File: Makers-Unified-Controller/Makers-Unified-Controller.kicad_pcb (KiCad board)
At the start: 2 copper layers, 160 x 83.8 mm, 62 parts, among them J1 USB_B_Micro, J2 backup_PROG, Q1 SI2305B-TP, Q2 MMBT3904, Q3 MMBT3904, SW1 SW_DPDT_x2, SW10 SW_Push, SW11 SW_Push, SW12 SW_Push, SW13 SW_Push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

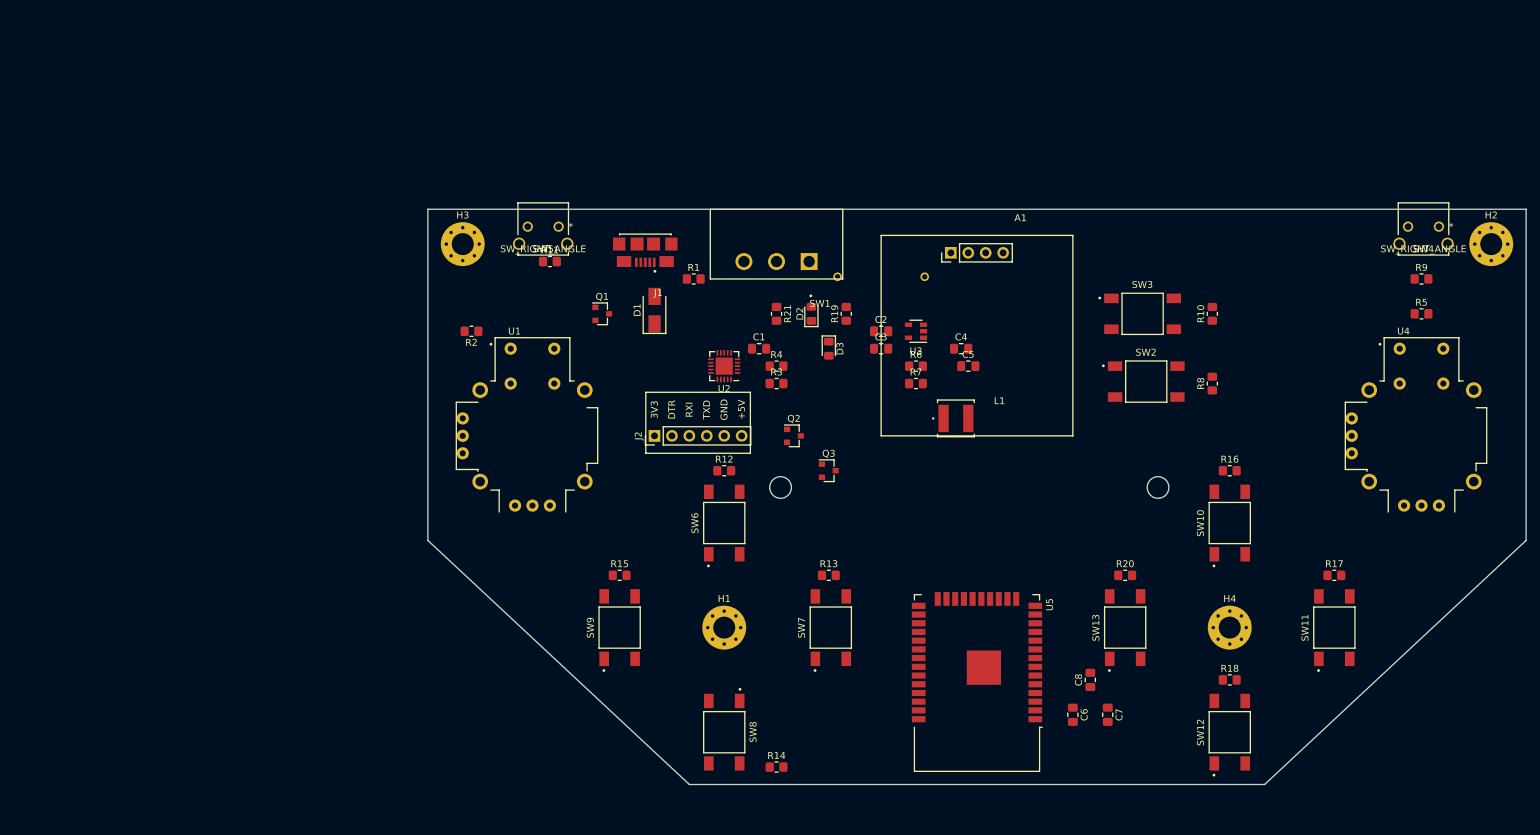
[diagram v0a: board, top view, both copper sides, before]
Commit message: Compacted layout
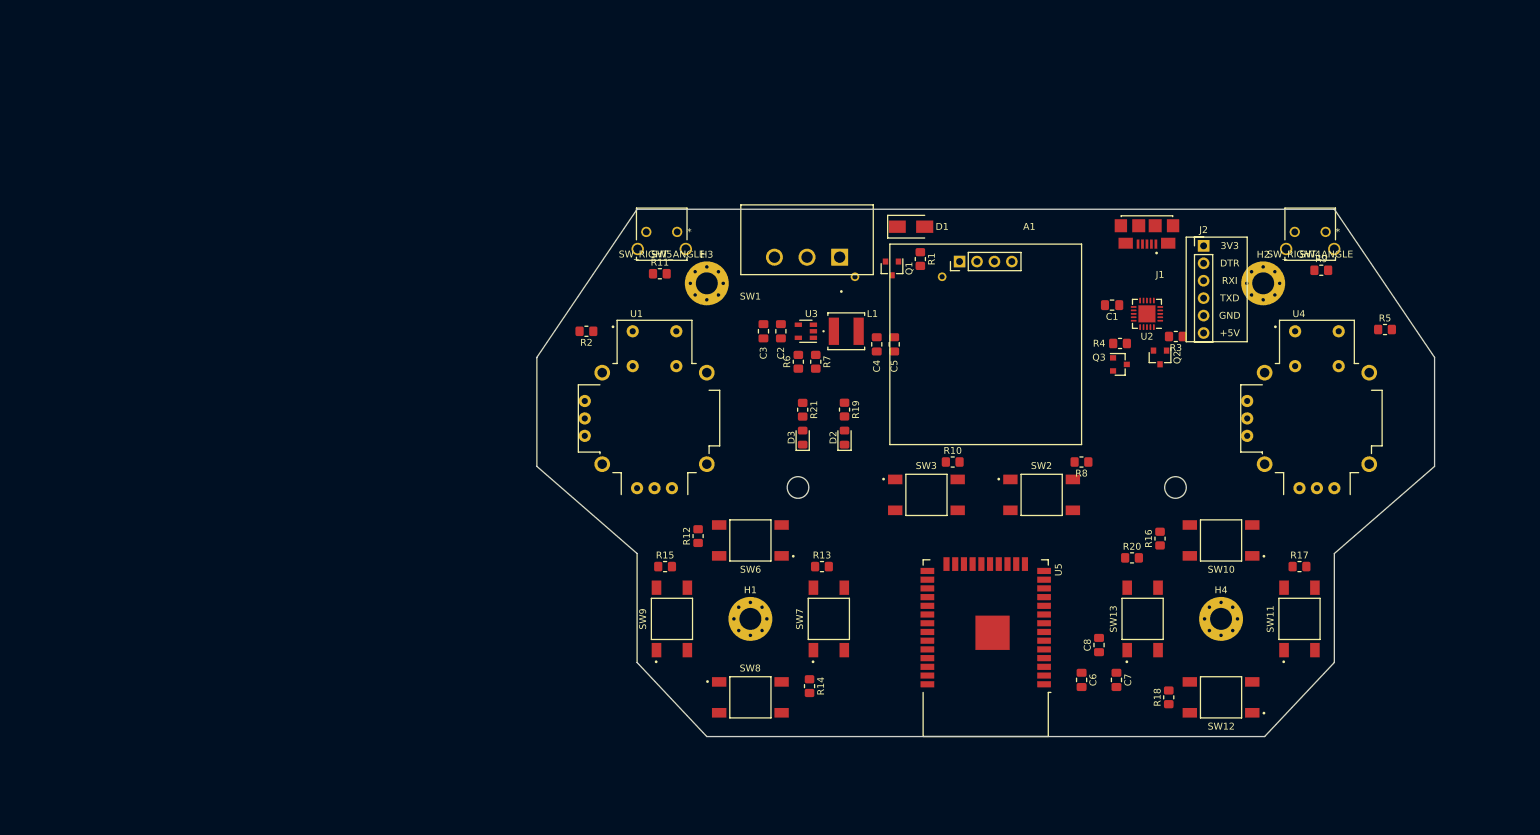
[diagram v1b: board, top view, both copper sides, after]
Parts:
- moved J2 84.7 mm to (193.0, 57.4), turned to 0 degrees
- moved J1 73.1 mm to (184.8, 57.1)
- moved U2 62.1 mm to (184.8, 67.3)
- moved R3 58.6 mm to (189.0, 70.6), turned to 180 degrees
- moved Q2 54.6 mm to (186.7, 73.7), turned to 270 degrees
- moved C1 51.8 mm to (179.7, 66.0), turned to 180 degrees
- moved R4 50.2 mm to (180.9, 71.6), turned to 180 degrees
- moved Q3 45.2 mm to (180.8, 74.7)
- moved R10 43.6 mm to (156.5, 88.9), turned to 0 degrees
- moved Q1 42.7 mm to (147.6, 60.7), turned to 270 degrees
- moved SW3 41.1 mm to (152.7, 93.7)
- moved D1 39.3 mm to (150.4, 54.6), turned to 0 degrees
- moved H3 36.0 mm to (120.7, 62.9)
- moved H2 33.7 mm to (201.7, 62.9)
- moved R1 33.1 mm to (151.8, 59.3), turned to 270 degrees
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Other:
- board size 160 x 83.8 mm -> 130.8 x 76.8 mm

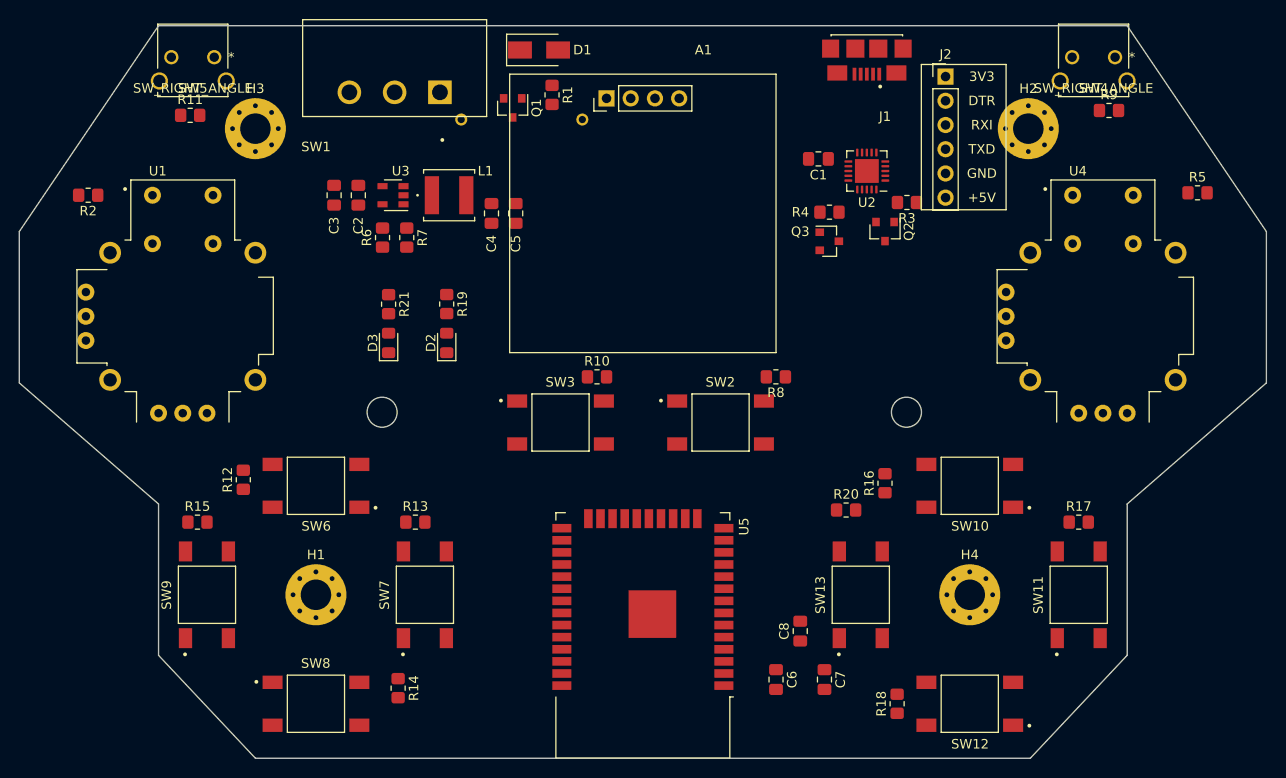
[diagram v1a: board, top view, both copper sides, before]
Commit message: Routed critical signals and power
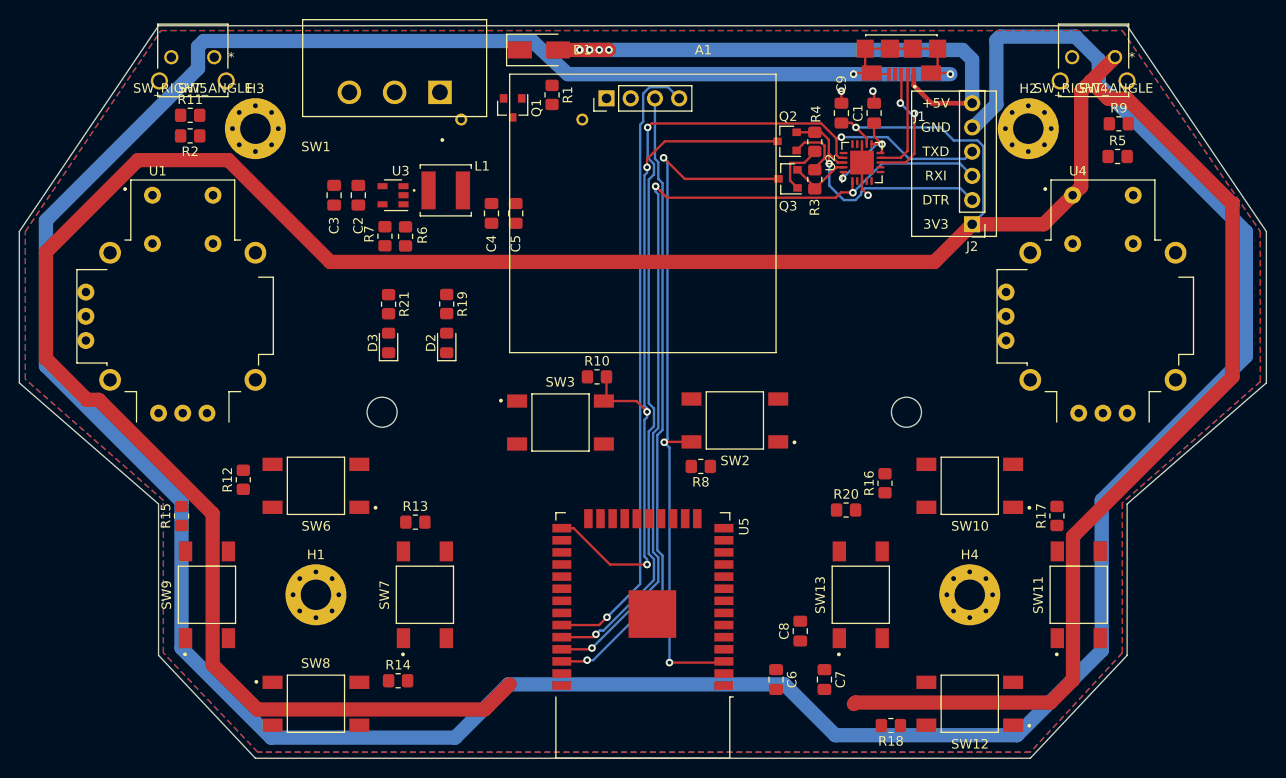
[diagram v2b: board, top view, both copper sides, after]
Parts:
- added C9: 1u, Capacitor_SMD:C_0805_2012Metric_Pad1.18x1.45mm_HandSolder, F.Cu at (182.1, 61.2)
- moved J2 15.7 mm to (195.8, 72.9), turned to 180 degrees
- moved Q2 14.0 mm to (176.4, 64.2), turned to 180 degrees
- moved R2 12.4 mm to (113.8, 63.6)
- moved R8 12.3 mm to (167.4, 98.3)
- moved R3 9.97 mm to (179.3, 68.2), turned to 90 degrees
- moved R5 9.21 mm to (211.1, 65.8)
- moved Q3 7.85 mm to (176.5, 68.1), turned to 180 degrees
- moved C1 7.56 mm to (185.5, 61.2), turned to 90 degrees
- moved R4 7.54 mm to (179.3, 64.2), turned to 270 degrees
- moved J1 3.63 mm to (188.4, 57.2)
- moved R6 2.42 mm to (136.4, 74.2)
- moved R18 2.38 mm to (187.3, 125.5), turned to 180 degrees
- moved R17 2.38 mm to (204.7, 103.5), turned to 90 degrees
- moved R7 2.29 mm to (134.2, 74.2)
- moved R15 1.79 mm to (112.9, 103.5), turned to 90 degrees
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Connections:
- net Net-(J1-Pad2) renamed /D-
- net Net-(J1-Pad3) renamed /D+
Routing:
- net GND: track 0.00 -> 388.9 mm, vias 0 -> 5
- net +3V3: track 0.00 -> 348.6 mm, vias 0 -> 1
- net /BRIDGE_TX: track 0.00 -> 99.6 mm, vias 0 -> 3
- net /BRIDGE_RX: track 0.00 -> 92.1 mm, vias 0 -> 3
- net /IO0: track 0.00 -> 75.6 mm, vias 0 -> 3
- net /EN: track 0.00 -> 75.1 mm, vias 0 -> 3
- net /I2C_SDA: track 0.00 -> 66.1 mm, vias 0 -> 1
- net /I2C_SCL: track 0.00 -> 66.1 mm, vias 0 -> 1
- net +5V: track 0.00 -> 59.5 mm, vias 0 -> 4
- net /BRIDGE_DTR: track 0.00 -> 27.3 mm, vias 0 -> 1
- net /D+: track 0.00 -> 13.2 mm, vias 0 -> 2
- net /D-: track 0.00 -> 11.2 mm
- net Net-(C1-Pad1): track 0.00 -> 10.8 mm, vias 0 -> 2
- net /BRIDGE_RTS: track 0.00 -> 6.70 mm
- net Net-(Q2-Pad1): track 0.00 -> 6.36 mm
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- added copper zone on F.Cu, net +3V3
- added copper zone on B.Cu, net GND

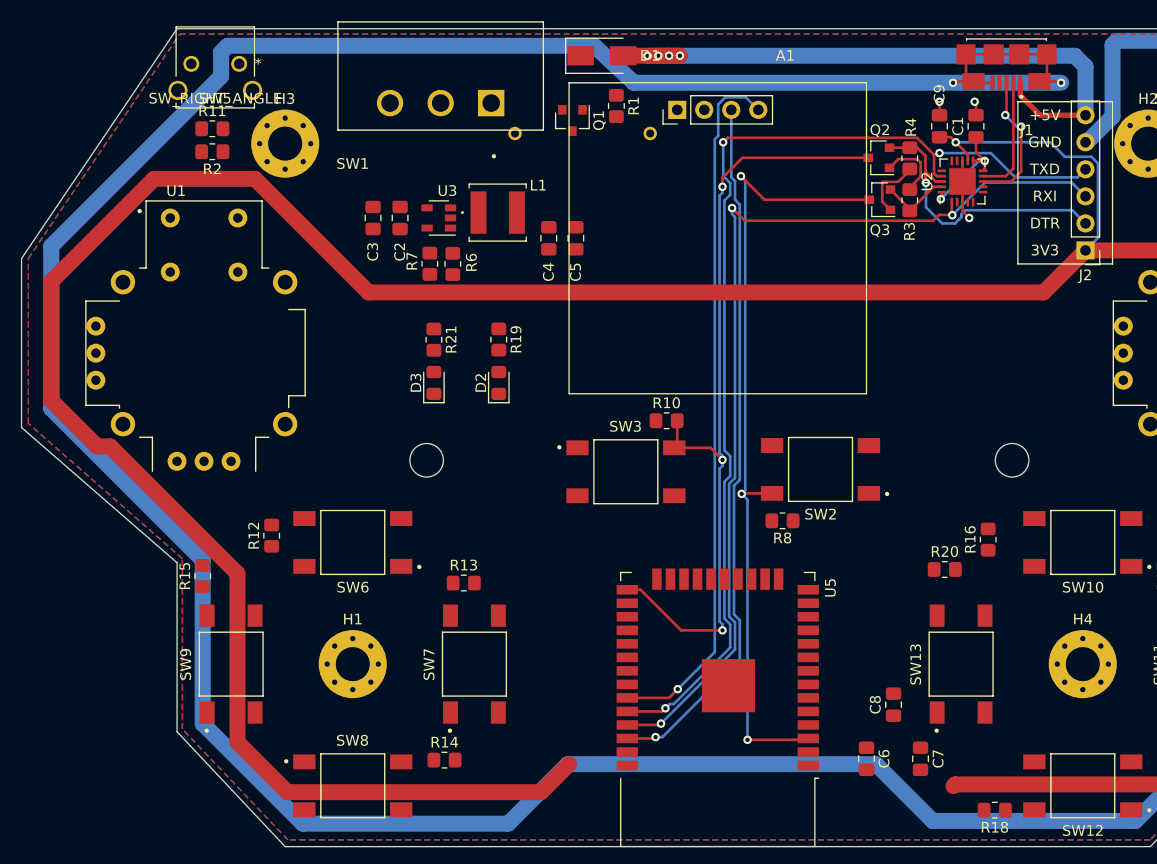
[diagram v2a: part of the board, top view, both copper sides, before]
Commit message: buck converter routing
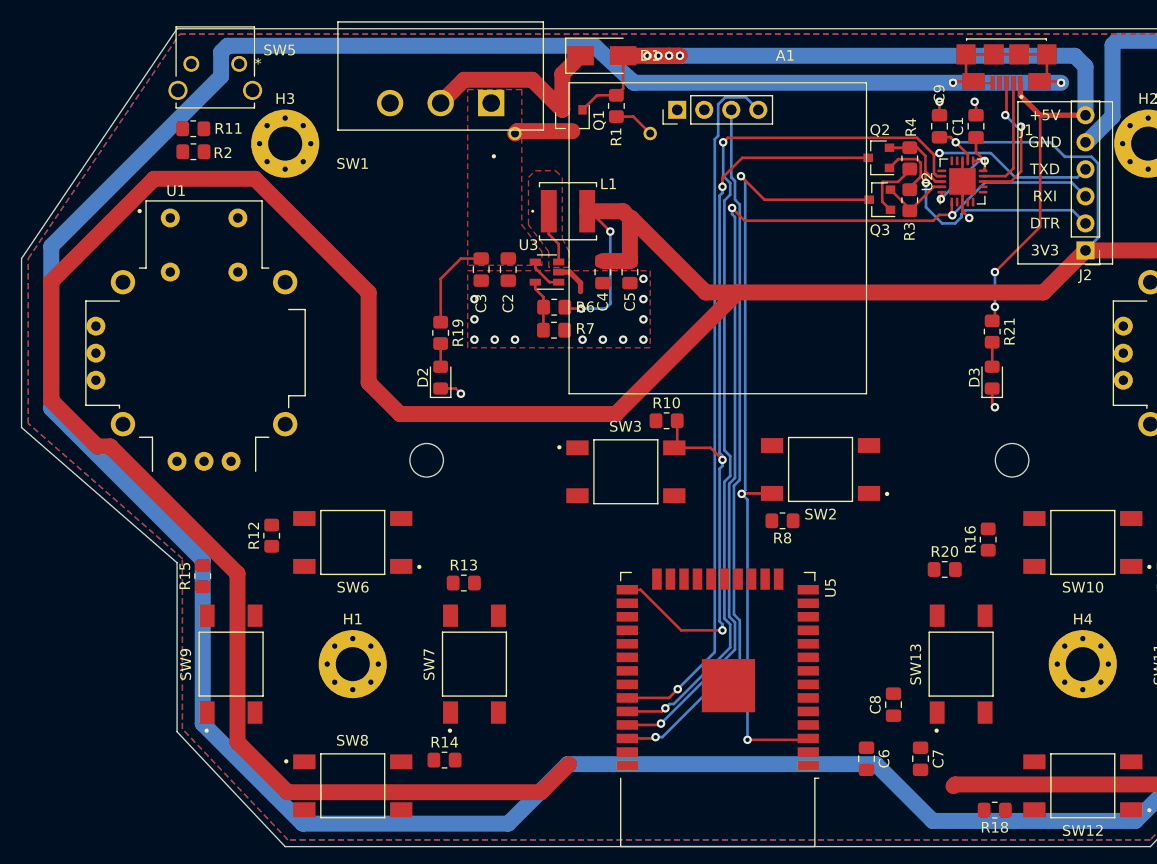
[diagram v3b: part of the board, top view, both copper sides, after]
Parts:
- moved R21 52.5 mm to (187.1, 80.5)
- moved D3 52.5 mm to (187.1, 84.8)
- moved R7 13.2 mm to (145.9, 80.4), turned to 0 degrees
- moved U3 11.4 mm to (145.2, 74.9)
- moved C2 11.3 mm to (141.6, 74.7)
- moved C3 11.3 mm to (139.1, 74.7)
- moved R6 10.4 mm to (145.9, 78.2), turned to 180 degrees
- moved L1 6.61 mm to (147.2, 69.2)
- moved C4 5.99 mm to (150.5, 74.9)
- moved C5 5.99 mm to (153.0, 74.9)
- moved R19 5.50 mm to (135.3, 80.6)
- moved D2 5.48 mm to (135.3, 84.8)
- moved R11 1.79 mm to (112.0, 61.5), turned to 180 degrees
- moved R2 1.78 mm to (112.0, 63.6)
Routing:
- net +3V3: track 348.6 -> 401.1 mm, vias 1 -> 3
- net +5V: track 59.5 -> 88.5 mm, vias 4 -> 6
- net Net-(D1-Pad1): track 0.00 -> 19.3 mm
- net /PWR_IN: track 0.00 -> 12.0 mm
- net GND: track 388.9 -> 400.0 mm, vias 5 -> 19
- net /BAT+: track 0.00 -> 5.49 mm
- net Net-(L1-Pad1): track 0.00 -> 5.15 mm
- net Net-(R6-Pad2): track 0.00 -> 4.83 mm
- net Net-(D3-Pad2): track 0.00 -> 2.30 mm
- net Net-(D2-Pad2): track 0.00 -> 2.17 mm
- added copper zone on F.Cu, net /PWR_IN
- added copper zone on F.Cu, net GND
- added copper zone on F.Cu, net Net-(L1-Pad1)

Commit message: Completed Routing
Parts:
- added C10: 1u, Capacitor_SMD:C_0805_2012Metric_Pad1.18x1.45mm_HandSolder, F.Cu at (148.8, 121.2)
- added C11: 1u, Capacitor_SMD:C_0805_2012Metric_Pad1.18x1.45mm_HandSolder, F.Cu at (169.7, 101.2)
- moved R18 15.3 mm to (200.4, 117.6), turned to 90 degrees
- moved R15 14.3 mm to (120.1, 115.8)
- moved R12 6.75 mm to (123.7, 104.9), turned to 0 degrees
- moved C8 5.58 mm to (173.5, 119.1), turned to 0 degrees
- moved R13 5.21 mm to (133.9, 107.9), turned to 270 degrees
- moved R14 4.95 mm to (131.0, 118.9), turned to 180 degrees
- moved C6 1.83 mm to (173.5, 121.2), turned to 0 degrees
- moved R16 1.80 mm to (188.5, 100.3)
- moved R20 1.55 mm to (182.9, 104.4)
- moved C7 1.13 mm to (179.3, 120.2)
- moved R8 0.85 mm to (167.0, 97.5)
- moved SW3 0.73 mm to (152.7, 93.0), turned to 180 degrees
- moved R10 0.51 mm to (156.5, 88.4)
- moved SW2 0.51 mm to (170.9, 93.0), turned to 0 degrees
- moved R11 0.25 mm to (112.0, 61.2)
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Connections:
- SW10 pad 2: /SW_5 -> (no net)
- SW10 pad 3: (no net) -> /SW_5
- SW11 pad 2: /SW_6 -> (no net)
- SW11 pad 3: (no net) -> /SW_6
- SW12 pad 2: /SW_7 -> (no net)
- SW12 pad 3: (no net) -> /SW_7
- SW13 pad 2: /SW_8 -> (no net)
- SW13 pad 3: (no net) -> /SW_8
- SW2 pad 2: /EN -> (no net)
- SW2 pad 3: (no net) -> /EN
- SW3 pad 2: /IO0 -> (no net)
- SW3 pad 3: (no net) -> /IO0
- SW6 pad 2: /SW_1 -> (no net)
- SW6 pad 3: (no net) -> /SW_1
- SW7 pad 2: /SW_2 -> (no net)
- SW7 pad 3: (no net) -> /SW_2
- SW8 pad 2: /SW_3 -> (no net)
- SW8 pad 3: (no net) -> /SW_3
- SW9 pad 2: /SW_4 -> (no net)
- SW9 pad 3: (no net) -> /SW_4
- U5 pad 10: /SW_6 -> /SW_5
- U5 pad 11: /SW_7 -> /SW_8
- U5 pad 12: /SW_8 -> /TRIG_R
- U5 pad 26: Net-(U5-Pad26) -> /LEFT_JOY_SW
- U5 pad 27: /SW_1 -> /SW_2
- U5 pad 28: /SW_2 -> /SW_1
- U5 pad 30: /SW_3 -> /SW_4
- U5 pad 31: /SW_4 -> /SW_3
- U5 pad 37: /SW_5 -> /TRIG_L
- U5 pad 4: Net-(U5-Pad4) -> /SW_7
- U5 pad 6: /TRIG_R -> /SW_6
- U5 pad 7: /TRIG_L -> /RIGHT_JOY_SW
- U5 pad 8: /RIGHT_JOY_Y -> /RIGHT_JOY_X
- U5 pad 9: /RIGHT_JOY_X -> /RIGHT_JOY_Y
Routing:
- net /TRIG_R: track 0.00 -> 86.2 mm, vias 0 -> 4
- net /TRIG_L: track 0.00 -> 86.1 mm, vias 0 -> 4
- net /RIGHT_JOY_SW: track 0.00 -> 76.7 mm, vias 0 -> 2
- net /LEFT_JOY_SW: track 0.00 -> 75.2 mm, vias 0 -> 3
- net /LEFT_JOY_X: track 0.00 -> 74.9 mm
- net /LEFT_JOY_Y: track 0.00 -> 74.0 mm
- net /RIGHT_JOY_Y: track 0.00 -> 62.8 mm, vias 0 -> 2
- net /RIGHT_JOY_X: track 0.00 -> 52.8 mm, vias 0 -> 2
- net GND: track 400.0 -> 445.9 mm, vias 19 -> 42
- net /SW_6: track 0.00 -> 41.7 mm
- net /SW_4: track 0.00 -> 37.5 mm
- net /SW_7: track 0.00 -> 37.1 mm
- net /SW_1: track 0.00 -> 35.1 mm
- net /SW_5: track 0.00 -> 27.5 mm
- net /SW_3: track 0.00 -> 26.7 mm
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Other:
- board text added: "BOOT"
- board text added: "EN"
- board text added: "Makers Unified Controller Rev. 1"
- board text added: "Power On Indicator"
- board text added: "USB PWR Indicator"
